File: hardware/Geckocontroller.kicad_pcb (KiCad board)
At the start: 2 copper layers, 114.3 x 96.5 mm, 101 parts, among them J101 AC Input, J11 I²C (BME280), J21 RGB LED, J31 DS18B20 I, J32 DS18B20 II, J40 FAN, J51 USB-C, J60 Load Cell Connector, J70 SPI / Addon Connector, J81 Dimmer, J91 Pump, J92 HeatBed, J93 HeatLamp, K81 AQG12212, K91 AQG12112, K92 AQG12112, K93 AQG12112, Q21 AO3400A, Q22 AO3400A, Q23 AO3400A, Q51 S8050, Q52 S8050, Q61 S8550, Q81 AO3400A, Q91 AO3400A, Q92 AO3400A, Q93 AO3400A, SW1 SW_Push, SW2 SW_Push, U1 ESP32-WROOM-32, U101 ACT4088, U2 CP2102, U61 HX711, U81 6N138

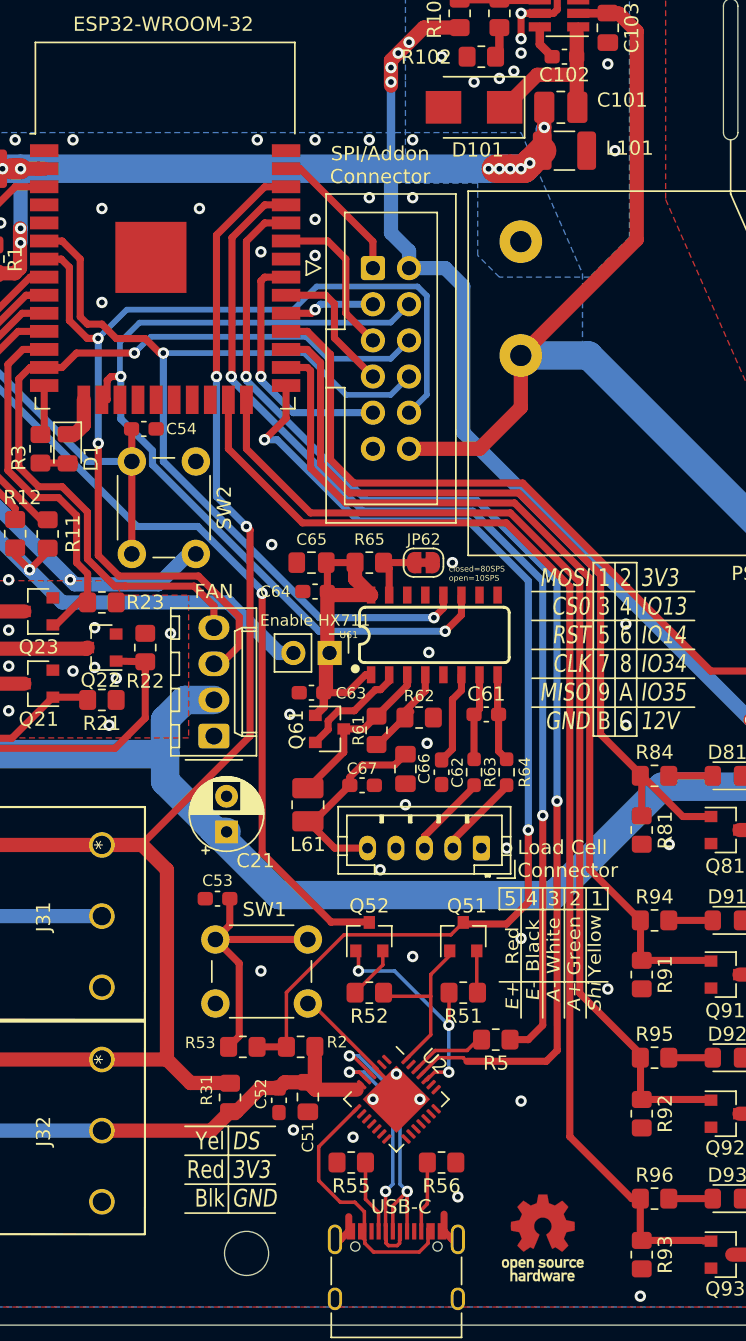
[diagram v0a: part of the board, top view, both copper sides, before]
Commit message: Hardware (Schema+PCB): Fix CP2102 power, optimize positionings
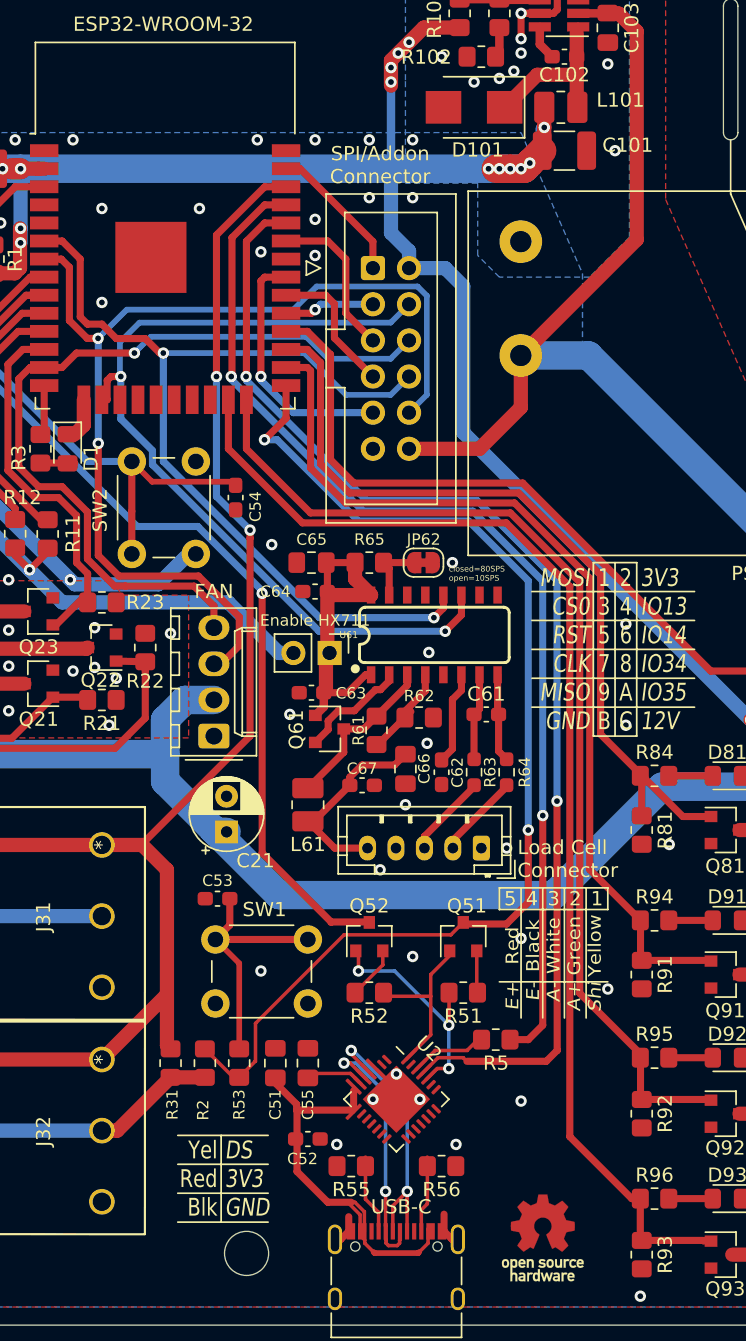
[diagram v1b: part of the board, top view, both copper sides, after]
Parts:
- added C55: 1µF, Capacitor_SMD:C_0805_2012Metric_Pad1.18x1.45mm_HandSolder, F.Cu at (47.5, 90.8)
- U2: footprint Package_DFN_QFN:QFN-28-1EP_5x5mm_P0.5mm_EP3.35x3.35mm -> Fraxinas:CP2102-QFN-28-modified
- moved C54 8.06 mm to (42.4, 51.1), turned to 270 degrees
- moved R2 6.83 mm to (40.3, 90.8), turned to 90 degrees
- moved R31 4.83 mm to (37.8, 90.8)
- moved C52 3.40 mm to (47.5, 96.1), turned to 0 degrees
- moved C51 3.30 mm to (45.2, 90.8), turned to 90 degrees
- moved R53 1.17 mm to (42.7, 90.8), turned to 270 degrees
- moved R55 0.25 mm to (50.5, 98.0)
- moved R56 0.25 mm to (56.9, 98.0)
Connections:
- C51 pad 1: +3V3 -> /VBUS
- C52 pad 1: +3V3 -> /VBUS
- U2 pad 6: +3V3 -> /VDD
- U2 pad 7: +3V3 -> /VBUS
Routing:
- net +3V3: track 293.9 -> 280.2 mm
- net /VBUS: track 18.5 -> 30.3 mm
- net GND: track 44.3 -> 37.5 mm, vias 73 -> 72
- net /Reset_switch: track 28.9 -> 34.4 mm
- net IO0: track 75.3 -> 80.0 mm
- net /VDD: track 0.00 -> 4.61 mm
- net /DS_in: track 98.9 -> 95.0 mm
- net /D-: track 17.9 -> 18.8 mm

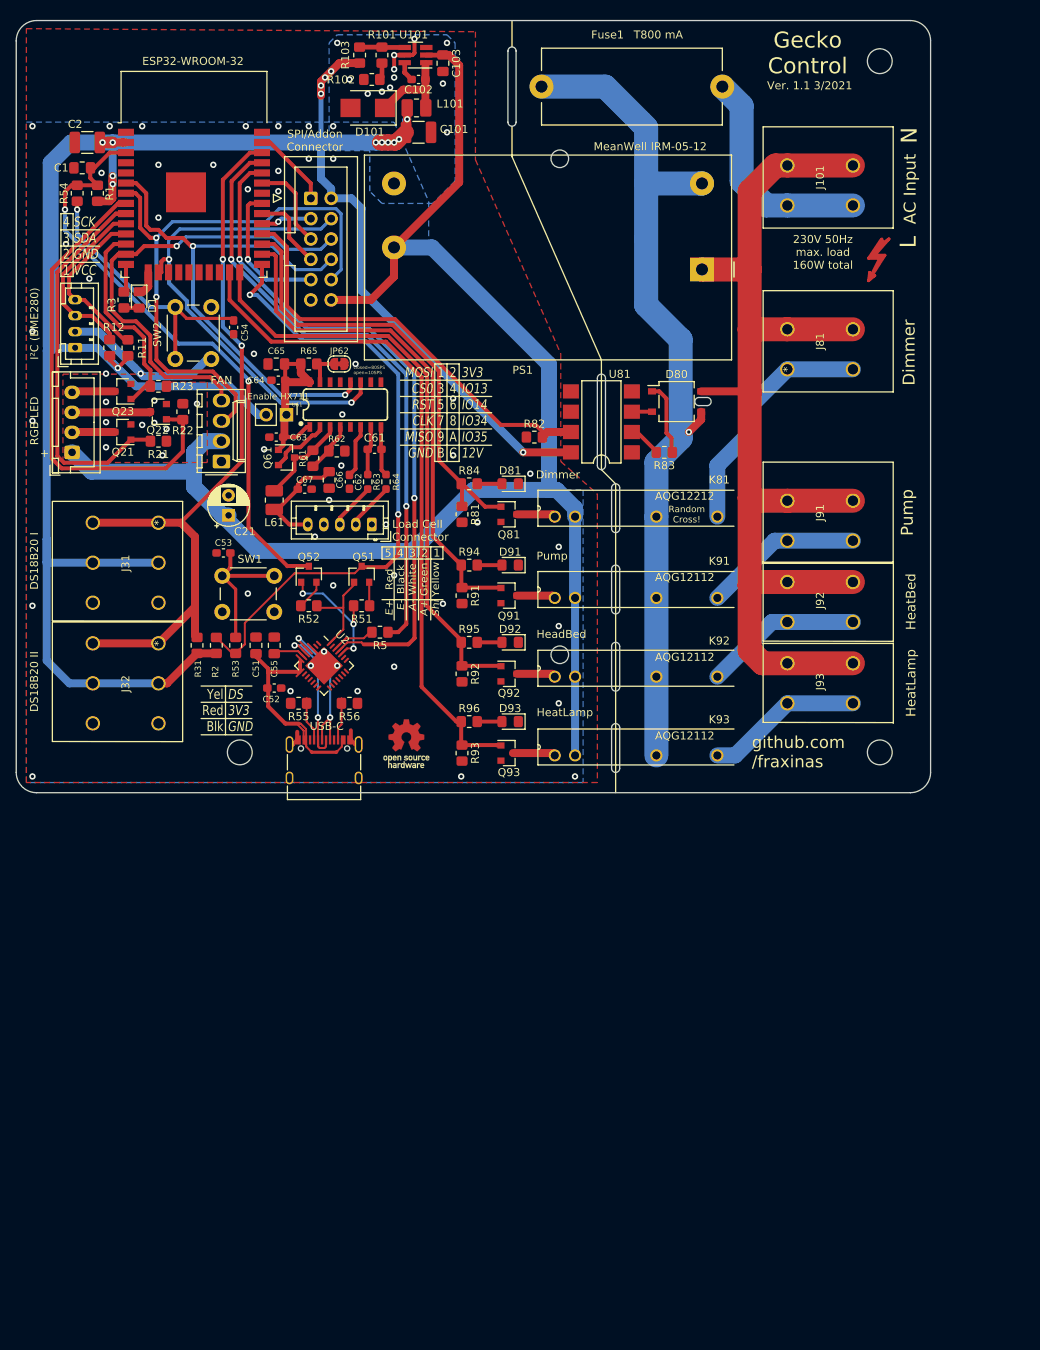
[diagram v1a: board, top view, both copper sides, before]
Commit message: hardware: Properly cross UART RX/TX connections
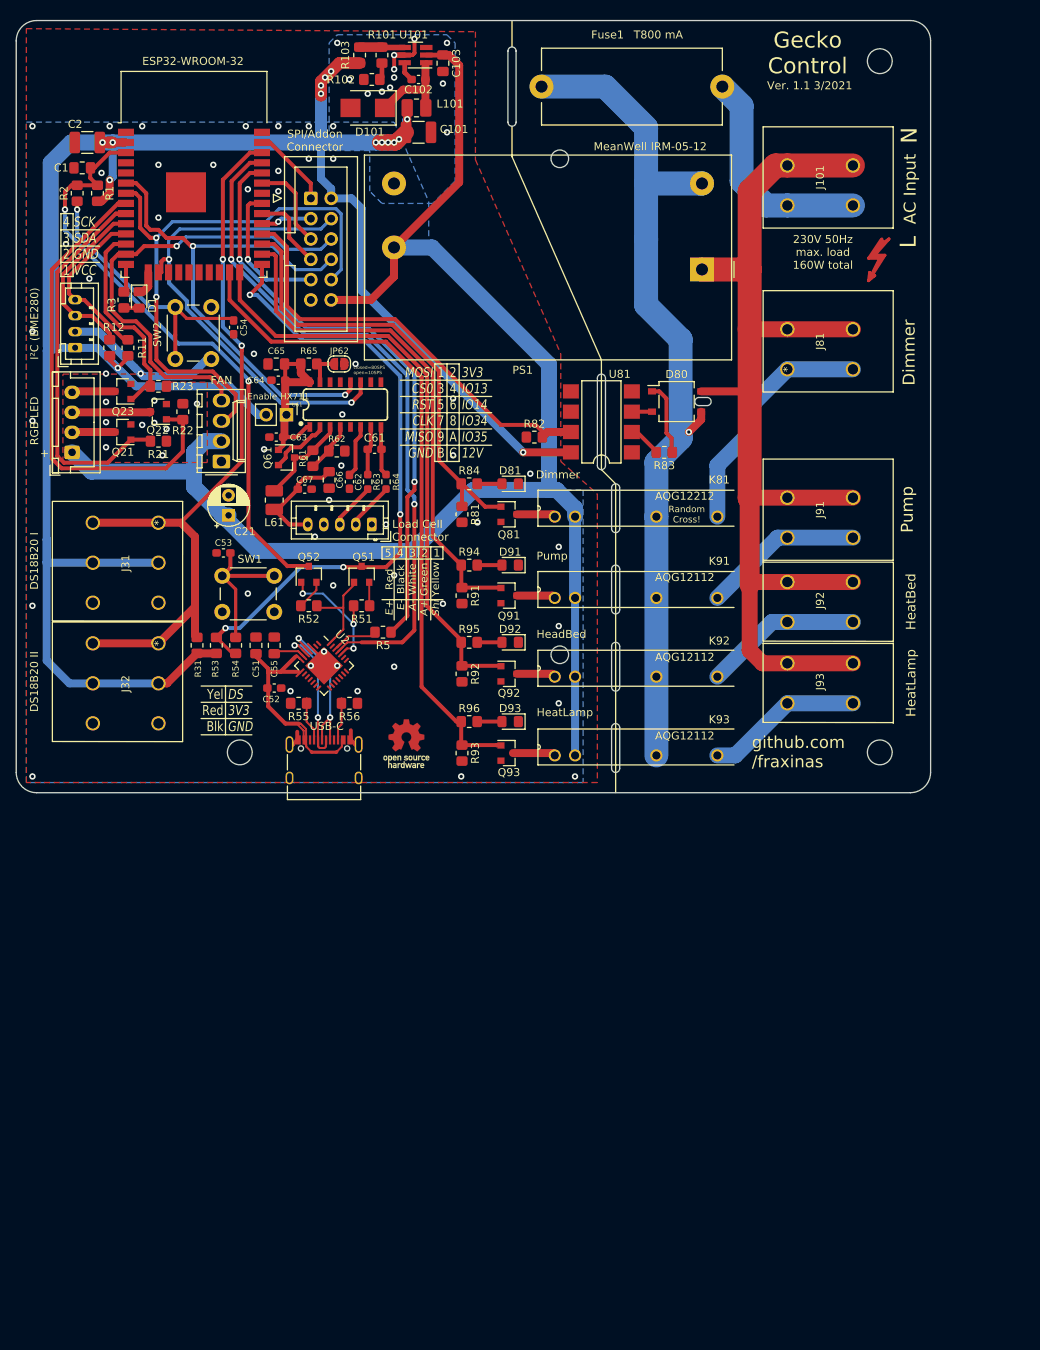
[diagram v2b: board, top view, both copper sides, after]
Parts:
- JP62: footprint Jumper:SolderJumper-2_P1.3mm_Bridged_RoundedPad1.0x1.5mm -> Jumper:SolderJumper-2_P1.3mm_Open_RoundedPad1.0x1.5mm
- moved J91 0.38 mm to (111.6, 77.3)
- moved R5 0.38 mm to (61.1, 89.2)
- renumbered R54 to R2, R2 to R53, R53 to R54
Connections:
- net TXD renamed RXD0'
- R5 pad 2: /TXD' -> /RXD0
- U1 pad 34: RXD -> /RXD0
- U1 pad 35: /TXD' -> TXD0
- U2 pad 25: RXD -> TXD0
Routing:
- net TXD0: track 0.00 -> 85.6 mm, vias 0 -> 2
- net RXD: track 84.3 -> 0.00 mm, vias 2 -> 0
- net /TXD': track 76.6 -> 0.00 mm, vias 2 -> 0
- net /RXD0: track 0.00 -> 74.2 mm, vias 0 -> 2
- net /VBUS: track 30.3 -> 31.9 mm
- net +3V3: track 280.2 -> 279.1 mm, vias 16 -> 15
- net IO0: track 80.0 -> 80.1 mm, vias 2 -> 4

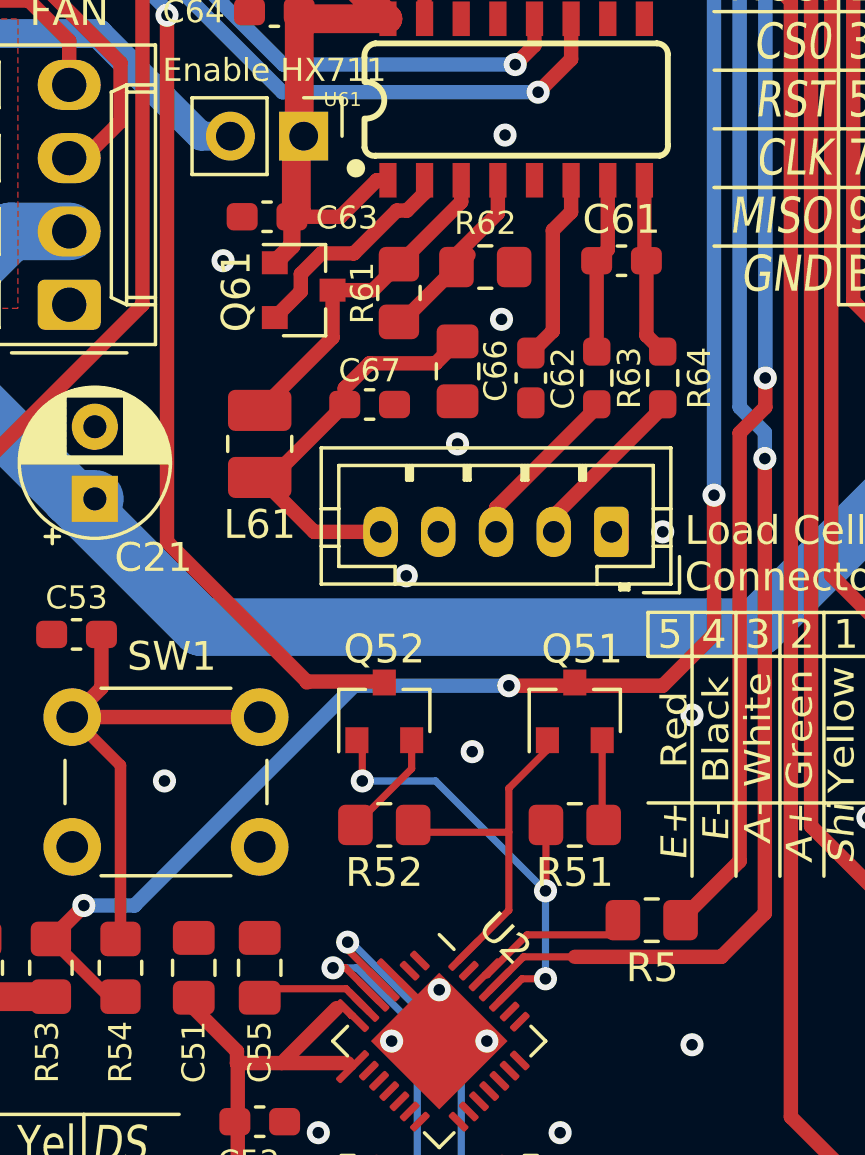
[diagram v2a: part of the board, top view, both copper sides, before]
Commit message: hardware: Add S8050 & S8550 symbols with fixed pinout
Fixes auto programming and HX711 Load Cell AVDD
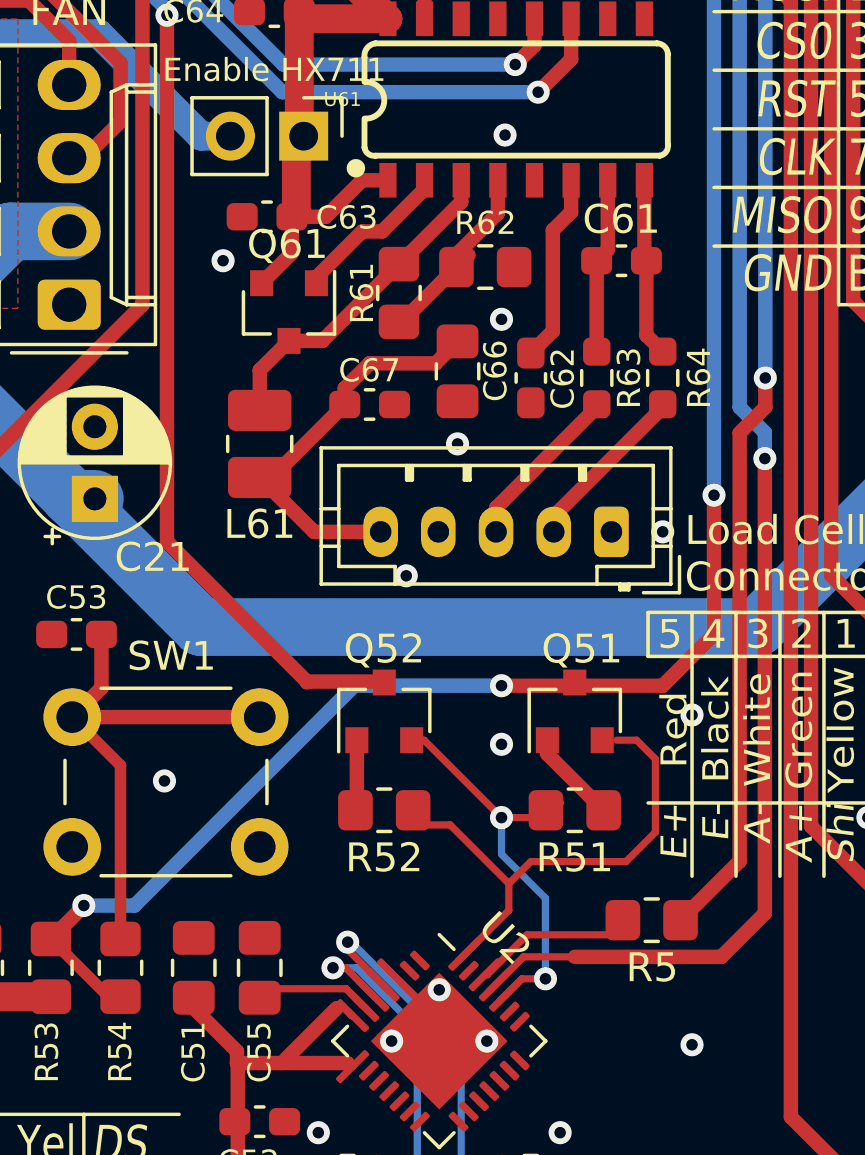
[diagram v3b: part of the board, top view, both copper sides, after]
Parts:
- moved Q61 0.91 mm to (48.5, 68.1), turned to 270 degrees
- moved R51 0.51 mm to (58.4, 85.3)
- moved R52 0.51 mm to (51.8, 85.3)
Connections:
- J51 pad A8: (no net) -> Net-(J51-PadA8)
- J51 pad B8: (no net) -> Net-(J51-PadB8)
- Q51 pad 1: /DTR -> Net-(Q51-Pad1)
- Q51 pad 2: Net-(Q51-Pad2) -> /DTR
- Q52 pad 1: /RTS -> Net-(Q52-Pad1)
- Q52 pad 2: Net-(Q52-Pad2) -> /RTS
- Q61 pad 1: Net-(C63-Pad1) -> Net-(Q61-Pad1)
- Q61 pad 2: Net-(Q61-Pad2) -> Net-(C63-Pad1)
- R51 pad 1: Net-(Q51-Pad2) -> Net-(Q51-Pad1)
- R52 pad 1: Net-(Q52-Pad2) -> Net-(Q52-Pad1)
- U1 pad 17: (no net) -> Net-(U1-Pad17)
- U1 pad 18: (no net) -> Net-(U1-Pad18)
- U1 pad 19: (no net) -> Net-(U1-Pad19)
- U1 pad 20: (no net) -> Net-(U1-Pad20)
- U1 pad 21: (no net) -> Net-(U1-Pad21)
- U1 pad 22: (no net) -> Net-(U1-Pad22)
- U1 pad 32: (no net) -> Net-(U1-Pad32)
- U1 pad 4: (no net) -> Net-(U1-Pad4)
- U1 pad 5: (no net) -> Net-(U1-Pad5)
- U101 pad 3: (no net) -> Net-(U101-Pad3)
- U2 pad 1: (no net) -> Net-(U2-Pad1)
- U2 pad 10: (no net) -> Net-(U2-Pad10)
- U2 pad 11: (no net) -> Net-(U2-Pad11)
- U2 pad 12: (no net) -> Net-(U2-Pad12)
- U2 pad 13: (no net) -> Net-(U2-Pad13)
- U2 pad 14: (no net) -> Net-(U2-Pad14)
- U2 pad 15: (no net) -> Net-(U2-Pad15)
- U2 pad 16: (no net) -> Net-(U2-Pad16)
- U2 pad 17: (no net) -> Net-(U2-Pad17)
- U2 pad 18: (no net) -> Net-(U2-Pad18)
- U2 pad 19: (no net) -> Net-(U2-Pad19)
- U2 pad 2: (no net) -> Net-(U2-Pad2)
- U2 pad 20: (no net) -> Net-(U2-Pad20)
- U2 pad 21: (no net) -> Net-(U2-Pad21)
- U2 pad 22: (no net) -> Net-(U2-Pad22)
- U2 pad 23: (no net) -> Net-(U2-Pad23)
- U2 pad 27: (no net) -> Net-(U2-Pad27)
- U2 pad 9: (no net) -> Net-(U2-Pad9)
- U61 pad 10: (no net) -> Net-(U61-Pad10)
- U61 pad 13: (no net) -> Net-(U61-Pad13)
- U61 pad 2: Net-(Q61-Pad2) -> Net-(Q61-Pad1)
- U61 pad 9: (no net) -> Net-(U61-Pad9)
- U81 pad 1: (no net) -> Net-(U81-Pad1)
- U81 pad 4: (no net) -> Net-(U81-Pad4)
- U81 pad 5: (no net) -> Net-(U81-Pad5)
- U81 pad 6: (no net) -> Net-(U81-Pad6)
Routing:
- net Net-(Q61-Pad2): track 7.78 -> 0.00 mm
- net Net-(Q61-Pad1): track 0.00 -> 5.52 mm
- net /DTR: track 12.4 -> 17.8 mm
- net Net-(Q52-Pad2): track 4.01 -> 0.00 mm
- net Net-(Q51-Pad1): track 0.00 -> 3.24 mm
- net Net-(Q51-Pad2): track 3.03 -> 0.00 mm
- net Net-(Q52-Pad1): track 0.00 -> 2.45 mm
- net /RTS: track 16.7 -> 14.6 mm, vias 3 -> 2
- net Net-(C63-Pad1): track 23.2 -> 23.8 mm

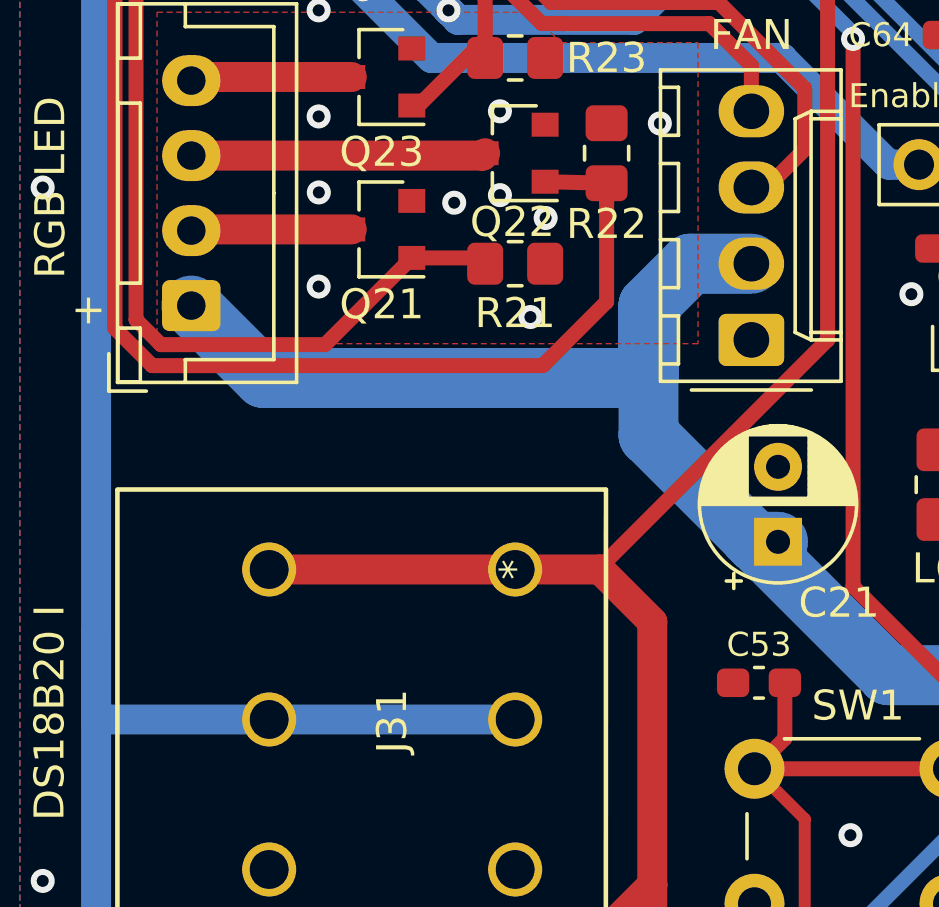
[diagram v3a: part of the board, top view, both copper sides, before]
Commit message: hardware: Add pullup R for Fan Tacho
GPIO35 doesn't seem to have in internal pullup resistor -
fixes fan tacho measurement
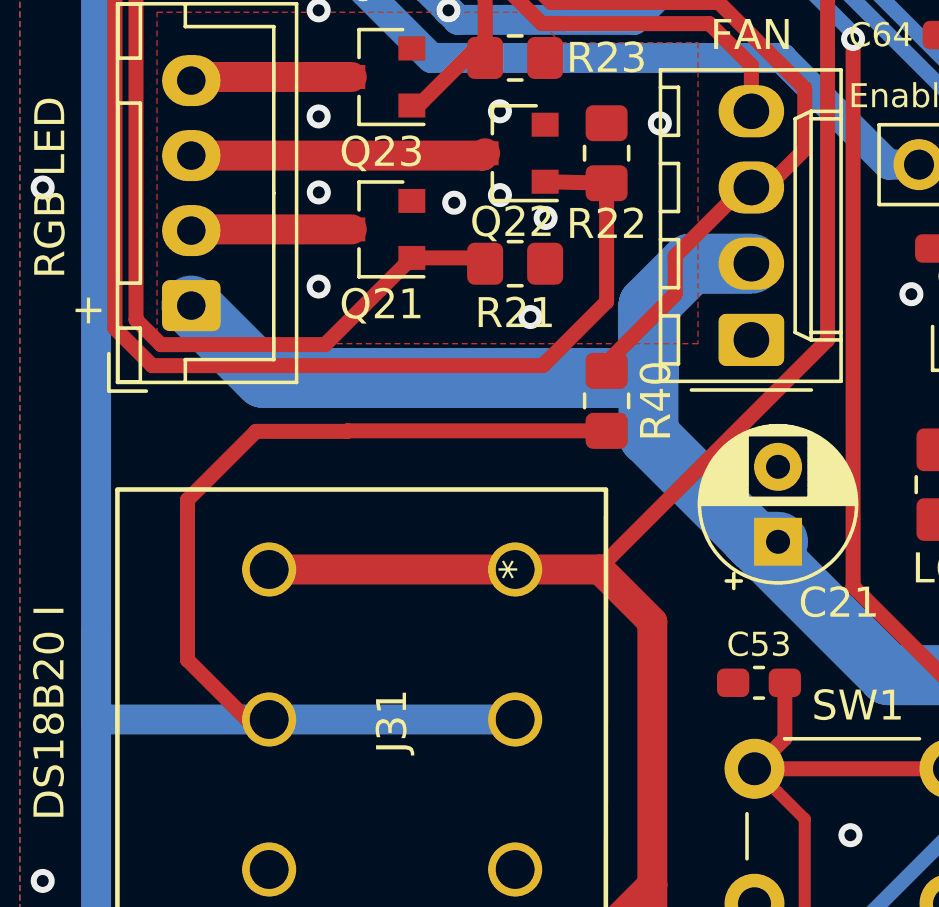
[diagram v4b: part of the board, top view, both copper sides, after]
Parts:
- added R40: 12k, Resistor_SMD:R_0805_2012Metric_Pad1.20x1.40mm_HandSolder, F.Cu at (36.1, 69.8)
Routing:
- net +3V3: track 279.1 -> 302.9 mm
- net FAN_SIG: track 73.8 -> 82.0 mm
